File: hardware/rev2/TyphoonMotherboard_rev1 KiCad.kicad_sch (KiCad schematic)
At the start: 74 parts, among them J1 Conn_02x04_Odd_Even, J2 Conn_01x04_Pin, J3 UJ20-C-H-C-4-SMT-TR, J5 Conn_01x02_Pin, J6 Conn_01x02_Pin, J7 Conn_01x04_Pin, SW1 SW_Push, SW2 SW_Push, SW3 SW_Push, U1 USBLC6-2SC6, U2 ESP32-S3-WROOM-1, U3 SN65HVD233, U4 BQ25895RTW, U5 TPS63802DLAR, U6 TPS63802DLAR

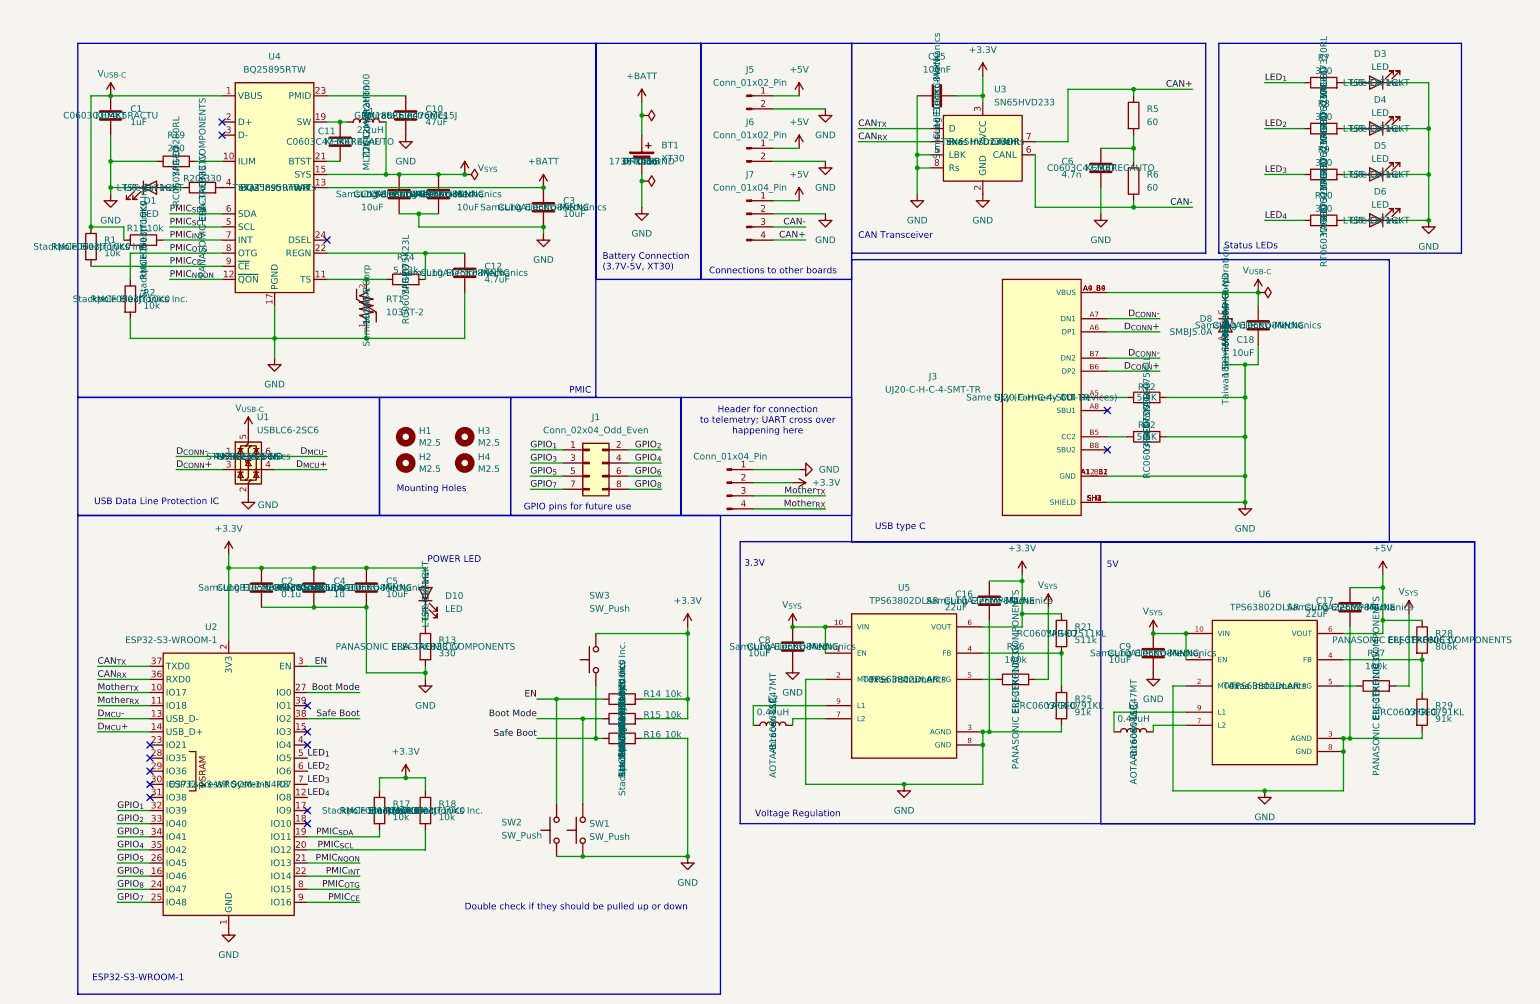
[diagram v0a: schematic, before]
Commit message: worked on pmic schematic
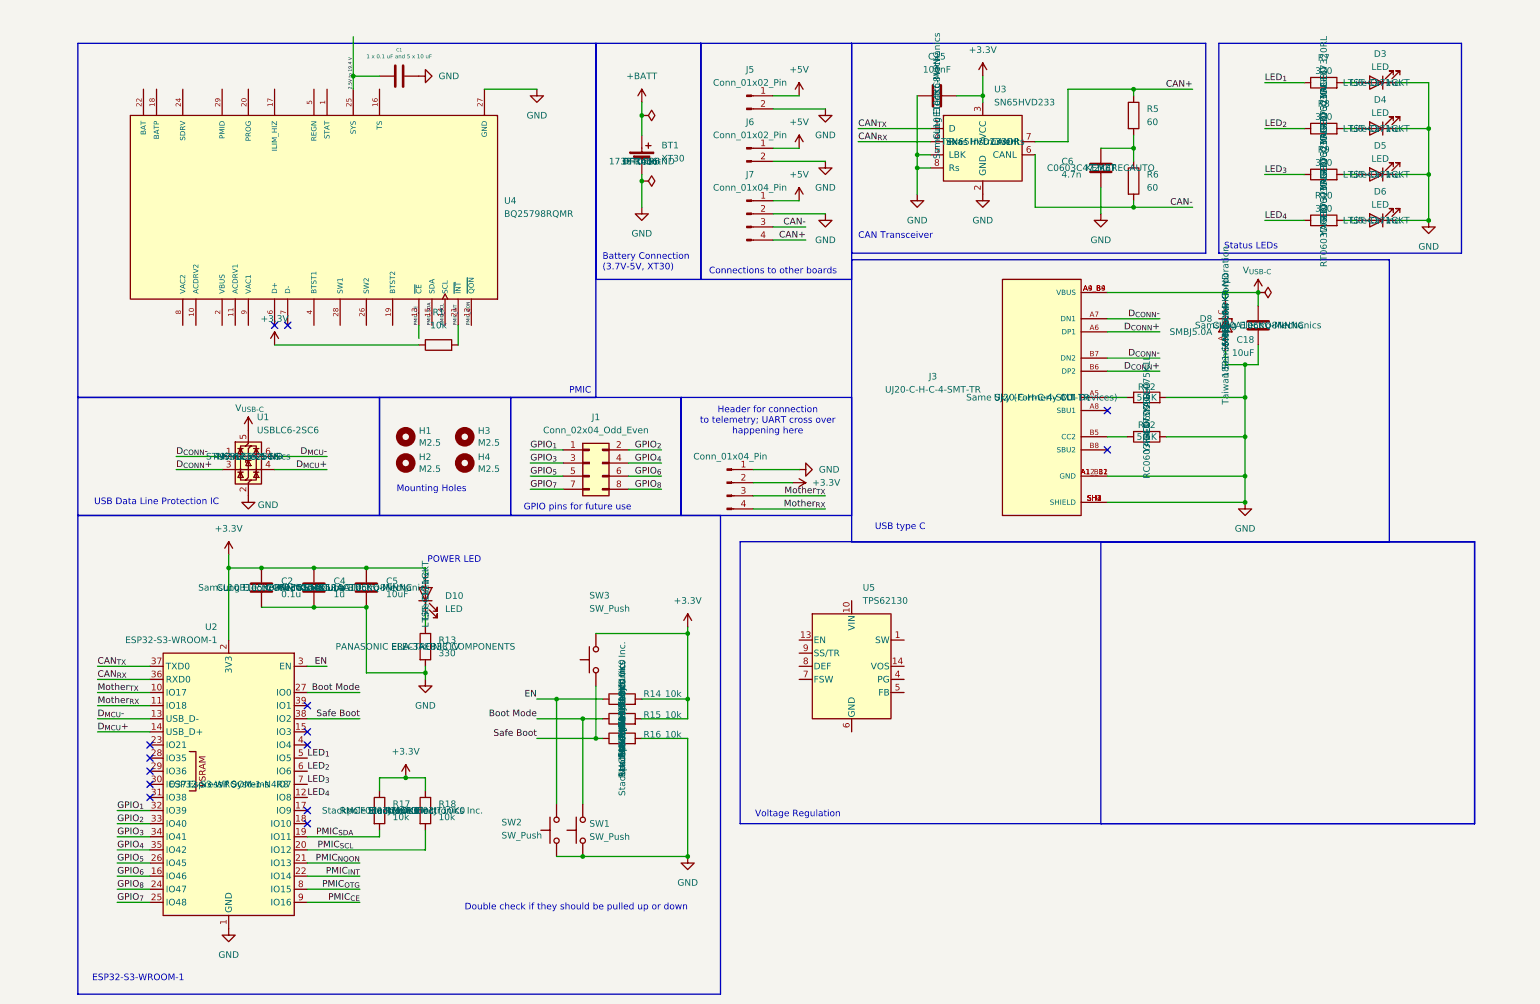
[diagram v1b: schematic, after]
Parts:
- removed C10: 47uF, Capacitor_SMD:C_0603_1608Metric, symbol Device:C
- removed C11: 47nF, Capacitor_SMD:C_0603_1608Metric, symbol Device:C
- removed C12: 4.7uF, Capacitor_SMD:C_0603_1608Metric, symbol Device:C
- removed C13, C14, C3, C8, C9: 10uF, Capacitor_SMD:C_0603_1608Metric, symbol Device:C
- removed C16, C17: 22uF, Capacitor_SMD:C_0603_1608Metric, symbol Device:C
- removed D1: LED, LED_SMD:LED_0805_2012Metric, symbol Device:LED
- removed L1: 2.2uH, Inductor_SMD:L_0805_2012Metric, symbol Device:L
- removed L2, L3: 0.47uH, Inductor_SMD:L_0603_1608Metric, symbol Device:L
- removed R11, R2: 10k, Resistor_SMD:R_0603_1608Metric, symbol Device:R
- removed R19: 280, Resistor_SMD:R_0603_1608Metric, symbol Device:R
- removed R20: 330, Resistor_SMD:R_0603_1608Metric, symbol Device:R
- removed R21: 511k, Resistor_SMD:R_0603_1608Metric, symbol Device:R
- removed R24: 5.23k, Resistor_SMD:R_0603_1608Metric, symbol Device:R
- removed R25, R29: 91k, Resistor_SMD:R_0603_1608Metric, symbol Device:R
- removed R26, R27: 100k, Resistor_SMD:R_0603_1608Metric, symbol Device:R
- removed R28: 806k, Resistor_SMD:R_0603_1608Metric, symbol Device:R
- removed RT1: 103AT-2, 103AT-2:103AT-2, symbol 103AT-2:103AT-2
- removed U4: BQ25895RTW, Package_DFN_QFN:Texas_RTW_WQFN-24-1EP_4x4mm_P0.5mm_EP2.7x2.7mm_ThermalVias, symbol Battery_Management:BQ25895RTW
- removed U5, U6: TPS63802DLAR, TPS63802DLAR (1):VREG_TPS63802DLAR, symbol TPS63802DLAR:TPS63802DLAR
- added U4: BQ25798RQMR, BQ25798RQMR:IC_BQ25798RQMR, symbol BQ25798RQMR:BQ25798RQMR
- added U5: TPS62130, Package_DFN_QFN:VQFN-16-1EP_3x3mm_P0.5mm_EP1.68x1.68mm_ThermalVias, symbol Regulator_Switching:TPS62130
- C1: value 1uF -> 1 x 0.1 uF and 5 x 10 uF; footprint Capacitor_SMD:C_0603_1608Metric -> (none); Manufacturer KEMET -> (none); Manufacturer Part Number C0603C104K5RACTU -> (none)
- R1: footprint Resistor_SMD:R_0603_1608Metric -> (none); Manufacturer Stackpole Electronics Inc. -> (none); Manufacturer Part Number RMCF0603JT10K0 -> (none)
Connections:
- net +3.3V: now also R1.1
- net GND: now also C1.1, U4.27 (GND); no longer C1.2
- net PMIC_{CE}: no longer R1.2
- net V_{USB-C}: no longer C1.1, R1.1
- new net: U5.1 (SW), U5.2 (SW), U5.3 (SW)
- new net: U5.10 (VIN), U5.11 (VIN), U5.12 (VIN)
- new net: U5.15 (GND), U5.16 (GND), U5.17 (GND), U5.6 (GND)
- new net: U4.2 (VBUS), U4.3 (VBUS)
- new net 2.5V to 19.4 V: C1.2, U4.25 (SYS)
- new net BAT: U4.22 (BAT), U4.23 (BAT)
- new net PMIC_CE: U4.13 (~{CE})
- new net PMIC_INT: R1.2, U4.21 (~{INT})
- new net PMIC_QON: U4.12 (~{QON})
- new net PMIC_SCL: U4.14 (SCL)
- new net PMIC_SDA: U4.15 (SDA)
- no-connect marks 15 -> 14
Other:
- note removed: "3.3V"
- note removed: "5V"

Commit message: pmic and voltage regulator schematic updates
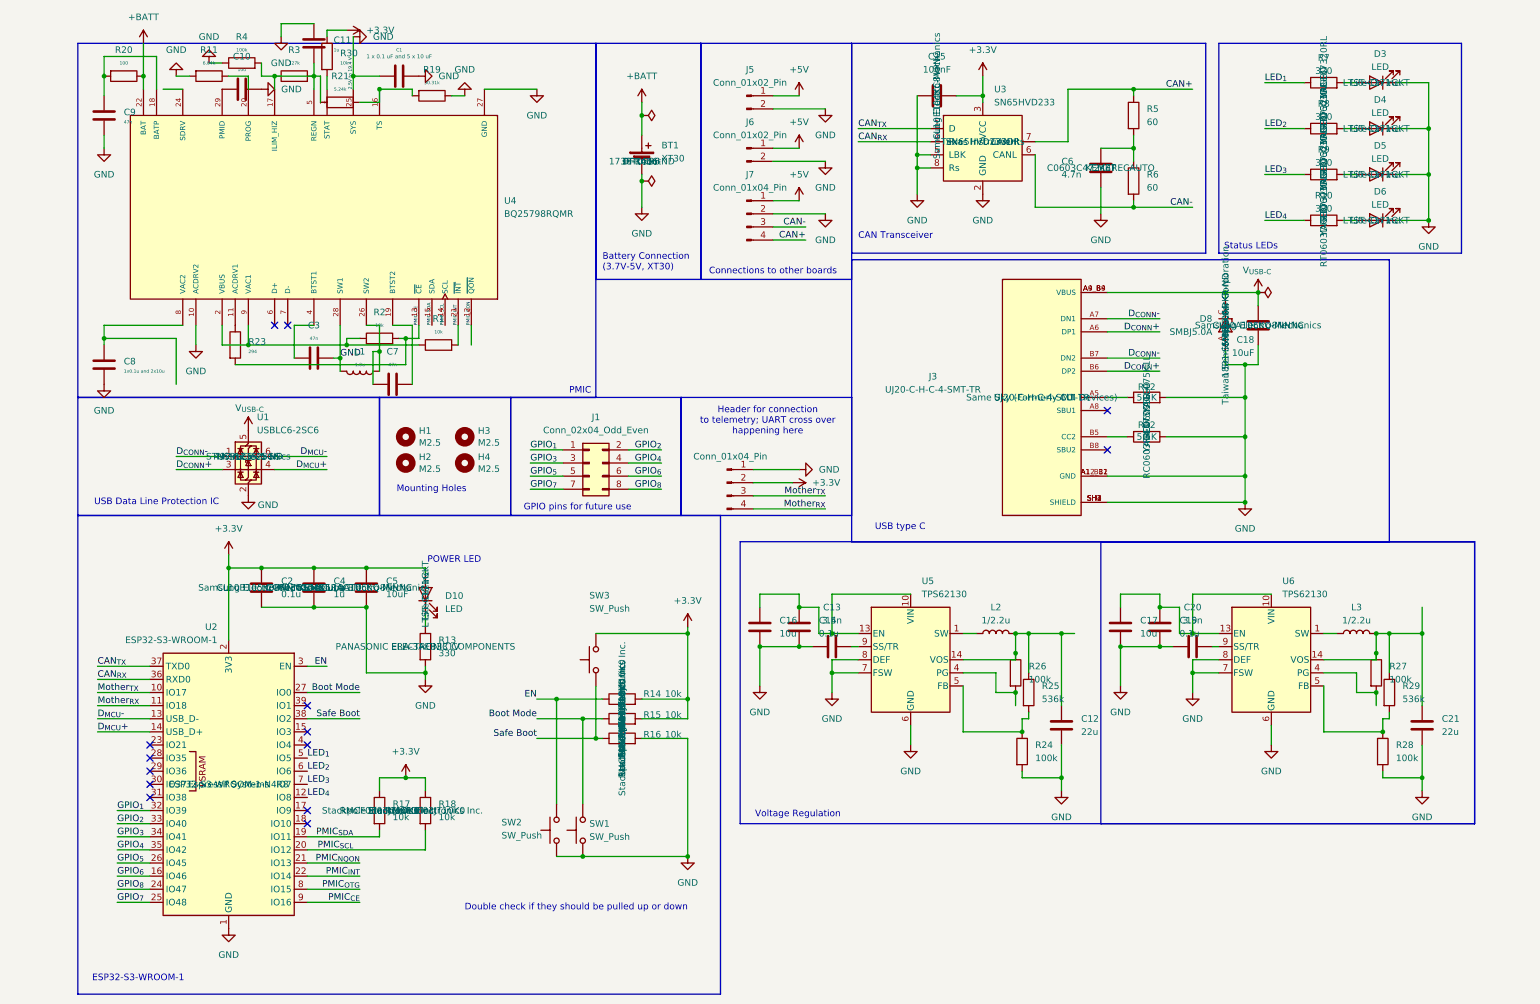
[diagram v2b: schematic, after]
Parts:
- added C10, C16, C17: 10u, symbol Device:C
- added C11: 1u, symbol Device:C
- added C12, C21: 22u, symbol Device:C
- added C13, C20: 3.5n, symbol Device:C
- added C14, C19: 0.1u, symbol Device:C
- added C3, C7, C9: 47n, symbol Device:C
- added C8: 1x0.1u and 2x10u, symbol Device:C
- added L1: 1.0u, symbol Device:L
- added L2, L3: 1/2.2u, symbol Device:L
- added R11: 6.04k, symbol Device:R
- added R19: 30.31k, symbol Device:R
- added R2, R30: 10k, symbol Device:R
- added R20: 100, symbol Device:R
- added R21: 5.24k, symbol Device:R
- added R23: 294, symbol Device:R
- added R24, R26, R27, R28, R4: 100k, symbol Device:R
- added R25, R29: 536k, symbol Device:R
- added R3: 127k, symbol Device:R
- added U6: TPS62130, Package_DFN_QFN:VQFN-16-1EP_3x3mm_P0.5mm_EP1.68x1.68mm_ThermalVias, symbol Regulator_Switching:TPS62130
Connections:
- net 2.5V to 19.4 V is gone; now on net GND: C1.2, U4.25 (SYS)
- net BAT is gone; now on net +BATT: U4.22 (BAT), U4.23 (BAT)
- net +3.3V: now also R30.1; no longer R1.1
- net +BATT: now also R20.1
- net GND: now also U4.10 (ACDRV2), U4.28 (SW1), U5.15 (GND), U5.16 (GND), U5.17 (GND), U5.6 (GND), U5.7 (FSW), U5.8 (DEF), C10.2, C11.1, C12.2, C13.1, C14.2, C16.2, C17.2, C19.2, C20.1, C21.2, C3.2, C8.2, C9.2, L1.2, R11.2, R19.1, R24.2, R28.2, R4.1, U6.15 (GND), U6.16 (GND), U6.17 (GND), U6.6 (GND), U6.7 (FSW), U6.8 (DEF)
- net PMIC_CE: now also R2.2, R23.2
- net at U5.1 (SW), U5.2 (SW), U5.3 (SW): now also L2.1
- net at U5.10 (VIN), U5.11 (VIN), U5.12 (VIN): now also U5.13 (EN), C14.1, C16.1
- net at U5.14 (VOS): now also C12.1, L2.2, R25.1, R26.1
- net at U5.4 (PG): now also R26.2
- net at U5.5 (FB): now also R24.1, R25.2
- net at U5.9 (SS/TR): now also C13.2
- net at U4.1 (STAT): now also R30.2
- net at U4.11 (ACDRV1): now also R23.1
- net at U4.16 (TS): now also R19.2, R21.2
- net at U4.17 (ILIM_HIZ): now also U4.5 (REGN), C11.2, R21.1, R3.1, R3.2, R4.2
- net at U4.18 (BATP): now also C9.1, R20.2
- net at U4.19 (BTST2): now also C7.2
- net at U4.2 (VBUS), U4.3 (VBUS): now also R1.1, U4.9 (VAC1), R2.1
- net at U4.20 (PROG): now also R11.1
- net at U4.26 (SW2): now also C7.1, L1.1
- net at U4.29 (PMID): now also C10.1
- net at U4.4 (BTST1): now also C3.1
- net at U4.8 (VAC2): now also C8.1
- new net: L3.1, U6.1 (SW), U6.2 (SW), U6.3 (SW)
- new net: C21.1, L3.2, R27.1, R29.1, U6.14 (VOS)
- new net: R27.2, U6.4 (PG)
- new net: C17.1, C19.1, U6.10 (VIN), U6.11 (VIN), U6.12 (VIN), U6.13 (EN)
- new net: R28.1, R29.2, U6.5 (FB)
- new net: C20.2, U6.9 (SS/TR)
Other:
- moved on the sheet: U5

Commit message: Reviewed the Schematic making PCB
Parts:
- removed D5, D6: LED, LED_SMD:LED_0805_2012Metric, symbol Device:LED
- removed R10, R9: 320, Resistor_SMD:R_0603_1608Metric, symbol Device:R
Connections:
- net LED_{3}: no longer names the net of U2.7 (IO7)
- net LED_{4}: no longer names the net of U2.12 (IO8)
- no-connect marks 14 -> 16
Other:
- moved on the sheet: D3, D4, R7, R8

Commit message: updates
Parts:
- R29: value 536k -> 312k
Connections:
- net PMIC_INT is gone; now on net PMIC_{INT}: R1.2, U4.21 (~{INT})
- net PMIC_QON is gone; now on net GND: U4.12 (~{QON})
- net PMIC_SCL is gone; now on net PMIC_{SCL}: U4.14 (SCL)
- net PMIC_SDA is gone; now on net PMIC_{SDA}: U4.15 (SDA)
- net PMIC_{CE}: now also R2.2, U4.13 (~{CE})
- net at R30.2, U4.1 (STAT): now also R21.1
- net at C11.2, R3.1, R3.2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: no longer R21.1
- net at R1.1, R2.1, U4.2 (VBUS)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: now also R23.2
- removed net PMIC_CE: R2.2, R23.2, U4.13 (~{CE})
- no-connect marks 16 -> 17
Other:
- moved on the sheet: C1, C10, C11, C3, C7, C8, C9, H1, H2, H3, H4, J1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

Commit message: removed updates
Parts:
- removed C10, C16, C17: 10u, symbol Device:C
- removed C11: 1u, symbol Device:C
- removed C12, C21: 22u, symbol Device:C
- removed C13, C20: 3.5n, symbol Device:C
- removed C14, C19: 0.1u, symbol Device:C
- removed C9: 47n, symbol Device:C
- removed L3: 1/2.2u, symbol Device:L
- removed R1, R2, R30: 10k, symbol Device:R
- removed R11: 6.04k, symbol Device:R
- removed R17, R18: 10k, Resistor_SMD:R_0603_1608Metric, symbol Device:R
- removed R19: 30.31k, symbol Device:R
- removed R20: 100, symbol Device:R
- removed R21: 5.24k, symbol Device:R
- removed R23: 294, symbol Device:R
- removed R24, R26, R27, R28, R4: 100k, symbol Device:R
- removed R25: 536k, symbol Device:R
- removed R29: 312k, symbol Device:R
- removed R3: 127k, symbol Device:R
- removed U4: BQ25798RQMR, BQ25798RQMR:IC_BQ25798RQMR, symbol BQ25798RQMR:BQ25798RQMR
- removed U5, U6: TPS62130, Package_DFN_QFN:VQFN-16-1EP_3x3mm_P0.5mm_EP1.68x1.68mm_ThermalVias, symbol Regulator_Switching:TPS62130
- added U4, U5: TPS62130A, Package_DFN_QFN:VQFN-16-1EP_3x3mm_P0.5mm_EP1.68x1.68mm_ThermalVias, symbol Regulator_Switching:TPS62130A
- C1: value 1 x 0.1 uF and 5 x 10 uF -> 10uF
- C3: value 47n -> 22uF
- C7: value 47n -> 10uF
- C8: value 1x0.1u and 2x10u -> 22uF
- L1: value 1.0u -> 2.2uH
- L2: value 1/2.2u -> 2.2uH
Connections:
- net +5V: now also C3.2, L1.2, U4.14 (VOS)
- net GND: now also C3.1, C7.1, C8.1; no longer C1.2, C3.2, C8.2, L1.2
- net V_{USB-C}: no longer C18.1, D8.C, J3.A4_B9 (VBUS), J3.A9_B4 (VBUS)
- net at L2.1: now also U5.1 (SW), U5.2 (SW), U5.3 (SW)
- net +3V3: now reaches L2.2
- net +3V3: now also C2.1, C4.1, C5.1, C8.2, D10.2 (A), J2.2 (Pin_2), R14.2, R15.2, SW3.2, U2.2 (3V3), U5.14 (VOS)
- net +6.2V: now reaches C7.2
- net +6.2V: now also U5.10 (VIN), U5.11 (VIN), U5.12 (VIN), U5.13 (EN)
- net at L1.1: now also U4.1 (SW), U4.2 (SW), U4.3 (SW); no longer C7.1
- removed net +3.3V: C15.2, C2.1, C4.1, C5.1, D10.2 (A), J2.2 (Pin_2), R14.2, R15.2, SW3.2, U2.2 (3V3), U3.3 (VCC)
- net PMIC_{CE}: no longer names the net of U2.9 (IO16)
- net PMIC_{INT}: no longer names the net of U2.22 (IO14)
- net PMIC_{NQON}: no longer names the net of U2.21 (IO13)
- net PMIC_{OTG}: no longer names the net of U2.8 (IO15)
- net PMIC_{SCL}: no longer names the net of U2.20 (IO12)
- net PMIC_{SDA}: no longer names the net of U2.19 (IO11)
- new net: U4.15 (GND), U4.16 (GND), U4.17 (GND), U4.6 (GND)
- new net: U5.15 (GND), U5.16 (GND), U5.17 (GND), U5.6 (GND)
- new net +3v3: C15.2, U3.3 (VCC)
- new net +6V2: C1.2, U4.10 (VIN), U4.11 (VIN), U4.12 (VIN), U4.13 (EN)
- new net V_USB-C: C18.1, D8.C, J3.A4_B9 (VBUS), J3.A9_B4 (VBUS)
- no-connect marks 17 -> 14
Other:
- note removed: "PMIC"
- moved on the sheet: BT1, C15, C18, C2, C4, C5, C6, D10, D3, D4, D8, H1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
